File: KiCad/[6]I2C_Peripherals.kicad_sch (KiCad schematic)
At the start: 11 parts, among them U600 PCF8563TS, Y600 32768Hz

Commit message: Manufacture files preparation
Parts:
- Brd600: now not fitted
- C601: Manufacturer Part Number CL10B104KB8NNNC -> CL10B104KA8NNNC
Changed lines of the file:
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@@
 		(dnp no)
 		(fields_autoplaced yes)
-		(property "Reference" "#PWR45"
+		(property "Reference" "#PWR045"
 			(at 123.19 44.45 0)
 			(effects
@@
 			(project "rpi_pico_media_board"
 				(path "/883c739e-d2a5-4bc8-a050-29a6043b4072/475bb6c4-6e20-4219-b5f0-3b0e927f6712"
-					(reference "#PWR45")
+					(reference "#PWR045")
 					(unit 1)
 				)
@@
 			)
 		)
-		(property "Manufacturer Product Number" ""
-			(at 116.84 53.34 0)
-			(effects
-				(font
-					(size 1.27 1.27)
-				)
-				(hide yes)
-			)
-		)
 		(property "Manufacturer Part Number" "CL10A106KP8NNNC"
 			(at 116.84 53.34 0)
@@
 		(on_board yes)
 		(dnp no)
-		(property "Reference" "#PWR43"
+		(property "Reference" "#PWR043"
 			(at 86.36 123.19 0)
 			(effects
@@
 			(project "rpi_pico_media_board"
 				(path "/883c739e-d2a5-4bc8-a050-29a6043b4072/475bb6c4-6e20-4219-b5f0-3b0e927f6712"
-					(reference "#PWR43")
+					(reference "#PWR043")
 					(unit 1)
 				)
@@
 		(on_board yes)
 		(dnp no)
-		(property "Reference" "#PWR46"
+		(property "Reference" "#PWR046"
 			(at 123.19 71.12 0)
 			(effects
@@
 			(project "rpi_pico_media_board"
 				(path "/883c739e-d2a5-4bc8-a050-29a6043b4072/475bb6c4-6e20-4219-b5f0-3b0e927f6712"
-					(reference "#PWR46")
+					(reference "#PWR046")
 					(unit 1)
 				)
@@
 			)
 		)
-		(property "Manufacturer Product Number" ""
-			(at 80.01 77.47 0)
-			(effects
-				(font
-					(size 1.27 1.27)
-				)
-				(hide yes)
-			)
-		)
 		(property "Manufacturer Part Number" "1N4148W"
 			(at 80.01 77.47 0)
@@
 			)
 		)
-		(property "Manufacturer Product Number" ""
-			(at 63.5 105.41 0)
-			(effects
-				(font
-					(size 1.27 1.27)
-				)
-				(hide yes)
-			)
-		)
 		(property "Manufacturer Part Number" "OK2EL89CJI-111YLC-32.768K"
 			(at 63.5 105.41 0)
@@
 		(dnp no)
 		(fields_autoplaced yes)
-		(property "Reference" "#PWR42"
+		(property "Reference" "#PWR042"
 			(at 63.5 123.19 0)
 			(effects
@@
 			(project "rpi_pico_media_board"
 				(path "/883c739e-d2a5-4bc8-a050-29a6043b4072/475bb6c4-6e20-4219-b5f0-3b0e927f6712"
-					(reference "#PWR42")
+					(reference "#PWR042")
 					(unit 1)
 				)
@@
 			)
 		)
-		(property "Manufacturer Product Number" ""
-			(at 129.54 53.34 0)
-			(effects
-				(font
-					(size 1.27 1.27)
-				)
-				(hide yes)
-			)
-		)
-		(property "Manufacturer Part Number" "CL10B104KB8NNNC"
+		(property "Manufacturer Part Number" "CL10B104KA8NNNC"
 			(at 129.54 53.34 0)
 			(effects
@@
 		(on_board yes)
 		(dnp no)
-		(property "Reference" "#PWR40"
+		(property "Reference" "#PWR040"
 			(at 41.91 86.36 0)
 			(effects
@@
 			(project "rpi_pico_media_board"
 				(path "/883c739e-d2a5-4bc8-a050-29a6043b4072/475bb6c4-6e20-4219-b5f0-3b0e927f6712"
-					(reference "#PWR40")
+					(reference "#PWR040")
 					(unit 1)
 				)
@@
 		(dnp no)
 		(fields_autoplaced yes)
-		(property "Reference" "#FLG6"
+		(property "Reference" "#FLG06"
 			(at 86.36 75.565 0)
 			(effects
@@
 			(project "rpi_pico_media_board"
 				(path "/883c739e-d2a5-4bc8-a050-29a6043b4072/475bb6c4-6e20-4219-b5f0-3b0e927f6712"
-					(reference "#FLG6")
+					(reference "#FLG06")
 					(unit 1)
 				)
@@
 		(dnp no)
 		(fields_autoplaced yes)
-		(property "Reference" "#PWR41"
+		(property "Reference" "#PWR041"
 			(at 50.8 123.19 0)
 			(effects
@@
 			(project "rpi_pico_media_board"
 				(path "/883c739e-d2a5-4bc8-a050-29a6043b4072/475bb6c4-6e20-4219-b5f0-3b0e927f6712"
-					(reference "#PWR41")
+					(reference "#PWR041")
 					(unit 1)
 				)
@@
 		(dnp no)
 		(fields_autoplaced yes)
-		(property "Reference" "#PWR47"
+		(property "Reference" "#PWR047"
 			(at 189.23 64.77 0)
 			(effects
@@
 			(project "rpi_pico_media_board"
 				(path "/883c739e-d2a5-4bc8-a050-29a6043b4072/475bb6c4-6e20-4219-b5f0-3b0e927f6712"
-					(reference "#PWR47")
+					(reference "#PWR047")
 					(unit 1)
 				)
@@
 			)
 		)
-		(property "Manufacturer Product Number" ""
-			(at 109.22 82.55 0)
-			(effects
-				(font
-					(size 1.27 1.27)
-				)
-				(hide yes)
-			)
-		)
 		(property "Manufacturer Part Number" "0805W8F5101T5E"
 			(at 109.22 82.55 0)
@@
 			)
 		)
-		(property "Manufacturer Product Number" ""
-			(at 50.8 110.49 0)
-			(effects
-				(font
-					(size 1.27 1.27)
-				)
-				(hide yes)
-			)
-		)
 		(property "Manufacturer Part Number" "CL10C150JB8NNNC"
 			(at 50.8 110.49 0)
@@
 		(on_board yes)
 		(dnp no)
-		(property "Reference" "#PWR48"
+		(property "Reference" "#PWR048"
 			(at 196.85 44.45 0)
 			(effects
@@
 			(project "rpi_pico_media_board"
 				(path "/883c739e-d2a5-4bc8-a050-29a6043b4072/475bb6c4-6e20-4219-b5f0-3b0e927f6712"
-					(reference "#PWR48")
+					(reference "#PWR048")
 					(unit 1)
 				)
@@
 			)
 		)
-		(property "Manufacturer Product Number" ""
-			(at 118.11 82.55 0)
-			(effects
-				(font
-					(size 1.27 1.27)
-				)
-				(hide yes)
-			)
-		)
 		(property "Manufacturer Part Number" "0805W8F5101T5E"
 			(at 118.11 82.55 0)
@@
 			)
 		)
-		(property "Manufacturer Product Number" ""
-			(at 86.36 96.52 0)
-			(effects
-				(font
-					(size 1.27 1.27)
-				)
-				(hide yes)
-			)
-		)
 		(property "Manufacturer Part Number" "PCF8563TS/5,118"
 			(at 86.36 96.52 0)
@@
 			)
 		)
-		(property "Manufacturer Product Number" ""
-			(at 92.71 77.47 0)
-			(effects
-				(font
-					(size 1.27 1.27)
-				)
-				(hide yes)
-			)
-		)
 		(property "Manufacturer Part Number" "1N4148W"
 			(at 92.71 77.47 0)
@@
 		(in_bom yes)
 		(on_board yes)
-		(dnp no)
+		(dnp yes)
 		(fields_autoplaced yes)
 		(property "Reference" "Brd600"
@@
 		(dnp no)
 		(fields_autoplaced yes)
-		(property "Reference" "#PWR44"
+		(property "Reference" "#PWR044"
 			(at 113.03 76.2 0)
 			(effects
@@
 			(project "rpi_pico_media_board"
 				(path "/883c739e-d2a5-4bc8-a050-29a6043b4072/475bb6c4-6e20-4219-b5f0-3b0e927f6712"
-					(reference "#PWR44")
-					(unit 1)
-				)
+					(reference "#PWR044")
+					(unit 1)
+				)

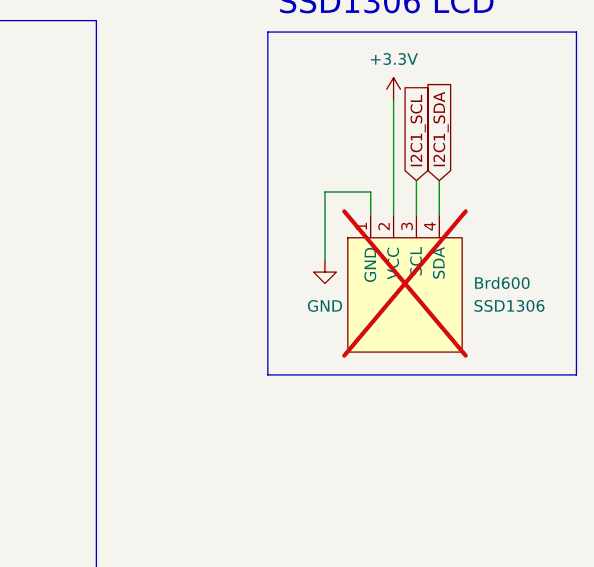
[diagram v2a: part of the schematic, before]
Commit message: Fixes for mic sample rate configuration
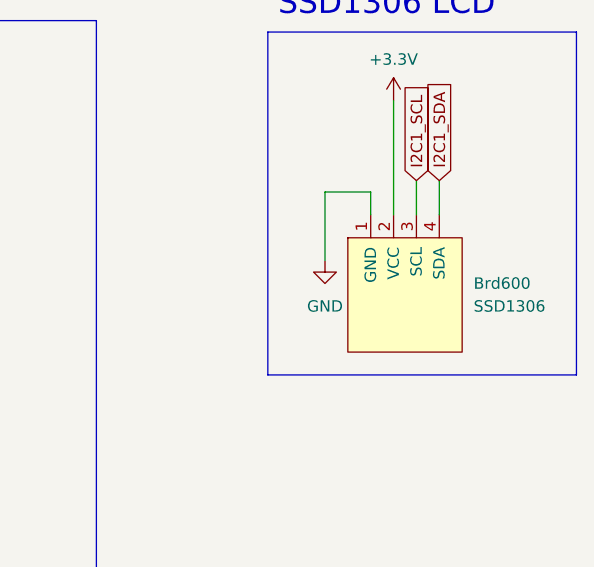
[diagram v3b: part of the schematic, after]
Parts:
- Brd600: now fitted
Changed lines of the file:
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@@
 		(in_bom yes)
 		(on_board yes)
-		(dnp yes)
+		(dnp no)
 		(fields_autoplaced yes)
 		(property "Reference" "Brd600"
